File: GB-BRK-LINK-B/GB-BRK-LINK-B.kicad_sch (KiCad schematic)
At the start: 6 parts

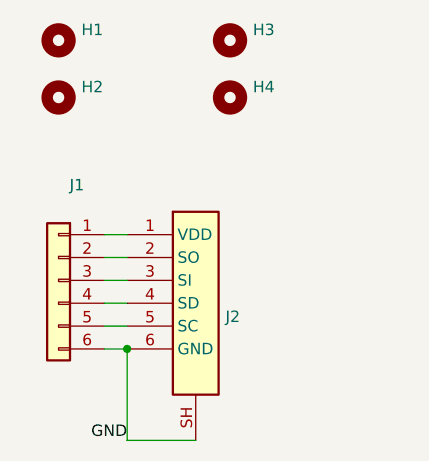
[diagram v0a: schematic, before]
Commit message: Upgrade projects to KiCad 7
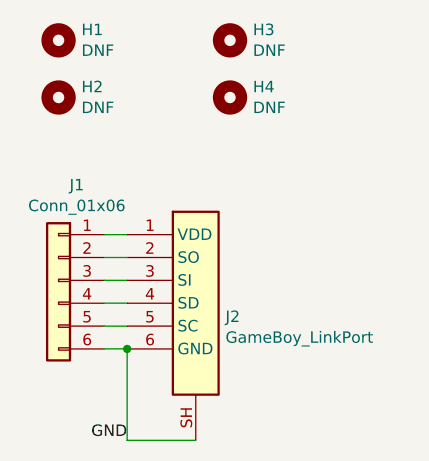
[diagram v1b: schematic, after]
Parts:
- H1, H2, H3, H4: value (none) -> DNF; footprint (none) -> MountingHole:MountingHole_3.2mm_M3
- J1: value (none) -> Conn_01x06; footprint (none) -> Connector_PinHeader_2.54mm:PinHeader_1x06_P2.54mm_Vertical
- J2: value (none) -> GameBoy_LinkPort; footprint (none) -> Gekkio_Connector:GameBoy_LinkPort_MGB_Horizontal
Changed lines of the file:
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@@
-(kicad_sch (version 20211123) (generator eeschema)
+(kicad_sch (version 20230121) (generator eeschema)
   (paper "A4")
   (title_block
@@
   )
   (wire (pts (xy 152.4 93.98) (xy 154.94 93.98))
-    (stroke (width 0) (type default) (color 0 0 0 0))
+    (stroke (width 0) (type default))
   )
   (wire (pts (xy 154.94 111.76) (xy 162.56 111.76))
-    (stroke (width 0) (type default) (color 0 0 0 0))
+    (stroke (width 0) (type default))
   )
   (wire (pts (xy 152.4 101.6) (xy 154.94 101.6))
-    (stroke (width 0) (type default) (color 0 0 0 0))
+    (stroke (width 0) (type default))
   )
   (wire (pts (xy 152.4 96.52) (xy 154.94 96.52))
-    (stroke (width 0) (type default) (color 0 0 0 0))
+    (stroke (width 0) (type default))
   )
   (wire (pts (xy 152.4 88.9) (xy 154.94 88.9))
-    (stroke (width 0) (type default) (color 0 0 0 0))
+    (stroke (width 0) (type default))
   )
   (wire (pts (xy 152.4 91.44) (xy 154.94 91.44))
-    (stroke (width 0) (type default) (color 0 0 0 0))
+    (stroke (width 0) (type default))
   )
   (wire (pts (xy 154.94 101.6) (xy 154.94 111.76))
-    (stroke (width 0) (type default) (color 0 0 0 0))
+    (stroke (width 0) (type default))
   )
   (wire (pts (xy 152.4 99.06) (xy 154.94 99.06))
-    (stroke (width 0) (type default) (color 0 0 0 0))
+    (stroke (width 0) (type default))
   )
-  (label "GND" (at 154.94 111.76 180)
+  (label "GND" (at 154.94 111.76 180) (fields_autoplaced)
     (effects (font (size 1.27 1.27)) (justify right bottom))
   )
   (symbol (lib_id "Gekkio_Connector_Specialized:GameBoy_LinkPort") (at 162.56 96.52 0) (unit 1)
-    (in_bom yes) (on_board yes)
-    (property "Reference" "J2" (id 0) (at 165.862 98.0186 0)
+    (in_bom yes) (on_board yes) (dnp no)
+    (property "Reference" "J2" (at 165.862 98.0186 0)
       (effects (font (size 1.27 1.27)) (justify left))
     )
-    (property "Value" "" (id 1) (at 165.862 100.33 0)
+    (property "Value" "GameBoy_LinkPort" (at 165.862 100.33 0)
       (effects (font (size 1.27 1.27)) (justify left))
     )
-    (property "Footprint" "" (id 2) (at 160.02 104.14 0)
+    (property "Footprint" "Gekkio_Connector:GameBoy_LinkPort_MGB_Horizontal" (at 160.02 104.14 0)
       (effects (font (size 1.27 1.27)) hide)
     )
-    (property "Datasheet" "" (id 3) (at 160.02 104.14 0)
+    (property "Datasheet" "" (at 160.02 104.14 0)
       (effects (font (size 1.27 1.27)) hide)
     )
@@
     (pin "6")
     (pin "SH")
+    (instances
+      (project "GB-BRK-LINK-B"
+        (path "/64c973ff-a7d9-4ea4-a8e2-d4d9977cab14"
+          (reference "J2") (unit 1)
+        )
+      )
+    )
   )
   (symbol (lib_id "Connector_Generic:Conn_01x06") (at 147.32 93.98 0) (mirror y) (unit 1)
-    (in_bom yes) (on_board yes)
-    (property "Reference" "J1" (id 0) (at 149.352 83.3882 0))
-    (property "Value" "" (id 1) (at 149.352 85.6996 0))
-    (property "Footprint" "" (id 2) (at 147.32 93.98 0)
+    (in_bom yes) (on_board yes) (dnp no)
+    (property "Reference" "J1" (at 149.352 83.3882 0)
+      (effects (font (size 1.27 1.27)))
+    )
+    (property "Value" "Conn_01x06" (at 149.352 85.6996 0)
+      (effects (font (size 1.27 1.27)))
+    )
+    (property "Footprint" "Connector_PinHeader_2.54mm:PinHeader_1x06_P2.54mm_Vertical" (at 147.32 93.98 0)
       (effects (font (size 1.27 1.27)) hide)
     )
-    (property "Datasheet" "~" (id 3) (at 147.32 93.98 0)
+    (property "Datasheet" "~" (at 147.32 93.98 0)
       (effects (font (size 1.27 1.27)) hide)
     )
@@
     (pin "5")
     (pin "6")
+    (instances
+      (project "GB-BRK-LINK-B"
+        (path "/64c973ff-a7d9-4ea4-a8e2-d4d9977cab14"
+          (reference "J1") (unit 1)
+        )
+      )
+    )
   )
   (symbol (lib_id "Mechanical:MountingHole") (at 147.32 67.31 0) (unit 1)
-    (in_bom yes) (on_board yes)
-    (property "Reference" "H1" (id 0) (at 149.86 66.1416 0)
+    (in_bom yes) (on_board yes) (dnp no)
+    (property "Reference" "H1" (at 149.86 66.1416 0)
       (effects (font (size 1.27 1.27)) (justify left))
     )
-    (property "Value" "" (id 1) (at 149.86 68.453 0)
+    (property "Value" "DNF" (at 149.86 68.453 0)
       (effects (font (size 1.27 1.27)) (justify left))
     )
-    (property "Footprint" "" (id 2) (at 147.32 67.31 0)
+    (property "Footprint" "MountingHole:MountingHole_3.2mm_M3" (at 147.32 67.31 0)
       (effects (font (size 1.27 1.27)) hide)
     )
-    (property "Datasheet" "~" (id 3) (at 147.32 67.31 0)
+    (property "Datasheet" "~" (at 147.32 67.31 0)
       (effects (font (size 1.27 1.27)) hide)
+    )
+    (instances
+      (project "GB-BRK-LINK-B"
+        (path "/64c973ff-a7d9-4ea4-a8e2-d4d9977cab14"
+          (reference "H1") (unit 1)
+        )
+      )
     )
   )
   (symbol (lib_id "Mechanical:MountingHole") (at 147.32 73.66 0) (unit 1)
-    (in_bom yes) (on_board yes)
-    (property "Reference" "H2" (id 0) (at 149.86 72.4916 0)
+    (in_bom yes) (on_board yes) (dnp no)
+    (property "Reference" "H2" (at 149.86 72.4916 0)
       (effects (font (size 1.27 1.27)) (justify left))
     )
-    (property "Value" "" (id 1) (at 149.86 74.803 0)
+    (property "Value" "DNF" (at 149.86 74.803 0)
       (effects (font (size 1.27 1.27)) (justify left))
     )
-    (property "Footprint" "" (id 2) (at 147.32 73.66 0)
+    (property "Footprint" "MountingHole:MountingHole_3.2mm_M3" (at 147.32 73.66 0)
       (effects (font (size 1.27 1.27)) hide)
     )
-    (property "Datasheet" "~" (id 3) (at 147.32 73.66 0)
+    (property "Datasheet" "~" (at 147.32 73.66 0)
       (effects (font (size 1.27 1.27)) hide)
+    )
+    (instances
+      (project "GB-BRK-LINK-B"
+        (path "/64c973ff-a7d9-4ea4-a8e2-d4d9977cab14"
+          (reference "H2") (unit 1)
+        )
+      )
     )
   )
   (symbol (lib_id "Mechanical:MountingHole") (at 166.37 67.31 0) (unit 1)
-    (in_bom yes) (on_board yes)
-    (property "Reference" "H3" (id 0) (at 168.91 66.1416 0)
+    (in_bom yes) (on_board yes) (dnp no)
+    (property "Reference" "H3" (at 168.91 66.1416 0)
       (effects (font (size 1.27 1.27)) (justify left))
     )
-    (property "Value" "" (id 1) (at 168.91 68.453 0)
+    (property "Value" "DNF" (at 168.91 68.453 0)
       (effects (font (size 1.27 1.27)) (justify left))
     )
-    (property "Footprint" "" (id 2) (at 166.37 67.31 0)
+    (property "Footprint" "MountingHole:MountingHole_3.2mm_M3" (at 166.37 67.31 0)
       (effects (font (size 1.27 1.27)) hide)
     )
-    (property "Datasheet" "~" (id 3) (at 166.37 67.31 0)
+    (property "Datasheet" "~" (at 166.37 67.31 0)
       (effects (font (size 1.27 1.27)) hide)
+    )
+    (instances
+      (project "GB-BRK-LINK-B"
+        (path "/64c973ff-a7d9-4ea4-a8e2-d4d9977cab14"
+          (reference "H3") (unit 1)
+        )
+      )
     )
   )
   (symbol (lib_id "Mechanical:MountingHole") (at 166.37 73.66 0) (unit 1)
-    (in_bom yes) (on_board yes)
-    (property "Reference" "H4" (id 0) (at 168.91 72.4916 0)
+    (in_bom yes) (on_board yes) (dnp no)
+    (property "Reference" "H4" (at 168.91 72.4916 0)
       (effects (font (size 1.27 1.27)) (justify left))
     )
-    (property "Value" "" (id 1) (at 168.91 74.803 0)
+    (property "Value" "DNF" (at 168.91 74.803 0)
       (effects (font (size 1.27 1.27)) (justify left))
     )
-    (property "Footprint" "" (id 2) (at 166.37 73.66 0)
+    (property "Footprint" "MountingHole:MountingHole_3.2mm_M3" (at 166.37 73.66 0)
       (effects (font (size 1.27 1.27)) hide)
     )
-    (property "Datasheet" "~" (id 3) (at 166.37 73.66 0)
+    (property "Datasheet" "~" (at 166.37 73.66 0)
       (effects (font (size 1.27 1.27)) hide)
+    )
+    (instances
+      (project "GB-BRK-LINK-B"
+        (path "/64c973ff-a7d9-4ea4-a8e2-d4d9977cab14"
+          (reference "H4") (unit 1)
+        )
+      )
     )
   )
@@
     (path "/" (page "1"))
   )
-  (symbol_instances
-    (path "/00000000-0000-0000-0000-00005bd2ef8b"
-      (reference "H1") (unit 1) (value "DNF") (footprint "MountingHole:MountingHole_3.2mm_M3")
-    )
-    (path "/00000000-0000-0000-0000-00005bd2efeb"
-      (reference "H2") (unit 1) (value "DNF") (footprint "MountingHole:MountingHole_3.2mm_M3")
-    )
-    (path "/00000000-0000-0000-0000-00005bd2f011"
-      (reference "H3") (unit 1) (value "DNF") (footprint "MountingHole:MountingHole_3.2mm_M3")
-    )
-    (path "/00000000-0000-0000-0000-00005bd2f055"
-      (reference "H4") (unit 1) (value "DNF") (footprint "MountingHole:MountingHole_3.2mm_M3")
-    )
-    (path "/00000000-0000-0000-0000-00005bd2ee6e"
-      (reference "J1") (unit 1) (value "Conn_01x06") (footprint "Connector_PinHeader_2.54mm:PinHeader_1x06_P2.54mm_Vertical")
-    )
-    (path "/00000000-0000-0000-0000-00005bd2ed76"
-      (reference "J2") (unit 1) (value "GameBoy_LinkPort") (footprint "Gekkio_Connector:GameBoy_LinkPort_MGB_Horizontal")
-    )
-  )
 )
